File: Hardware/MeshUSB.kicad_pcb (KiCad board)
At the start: 2 copper layers, 30.4 x 40.8 mm, 37 parts, among them P1 USB_4, P2 PVCell, Q1 MOS_P, U1 XBEE, U3 LTC3105-MSOP12, U4 FT231X-SSOP, U5 LTC4070

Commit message: Getting moving on v0.2 :)
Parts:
- L1: footprint SM1210 -> SM0805
- R10: value R -> 270
- U4: footprint SSOP20 -> _MUSB_SSOP20
- moved L1 34.7 mm to (137.2, 90.2)
- moved U4 21.2 mm to (166.6, 132.8)
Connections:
- F1 pad 1: N-0000015 -> N-0000012
- P1 pad 1: N-0000015 -> GND
- P1 pad 3: N-0000012 -> N-0000014
- P1 pad 4: GND -> N-0000012
- R1 pad 1: N-0000013 -> N-0000014
- R2 pad 1: N-0000012 -> N-0000013
- VR1 pad 1: N-0000012 -> N-0000013
- VR2 pad 1: N-0000013 -> N-0000014
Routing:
- net N-0000012: track 16.9 -> 3.61 mm
- net N-0000015: track 11.9 -> 0.00 mm
- net N-0000013: track 13.5 -> 2.69 mm
- net GND: track 173.4 -> 163.5 mm
- net N-0000014: track 0.00 -> 1.14 mm

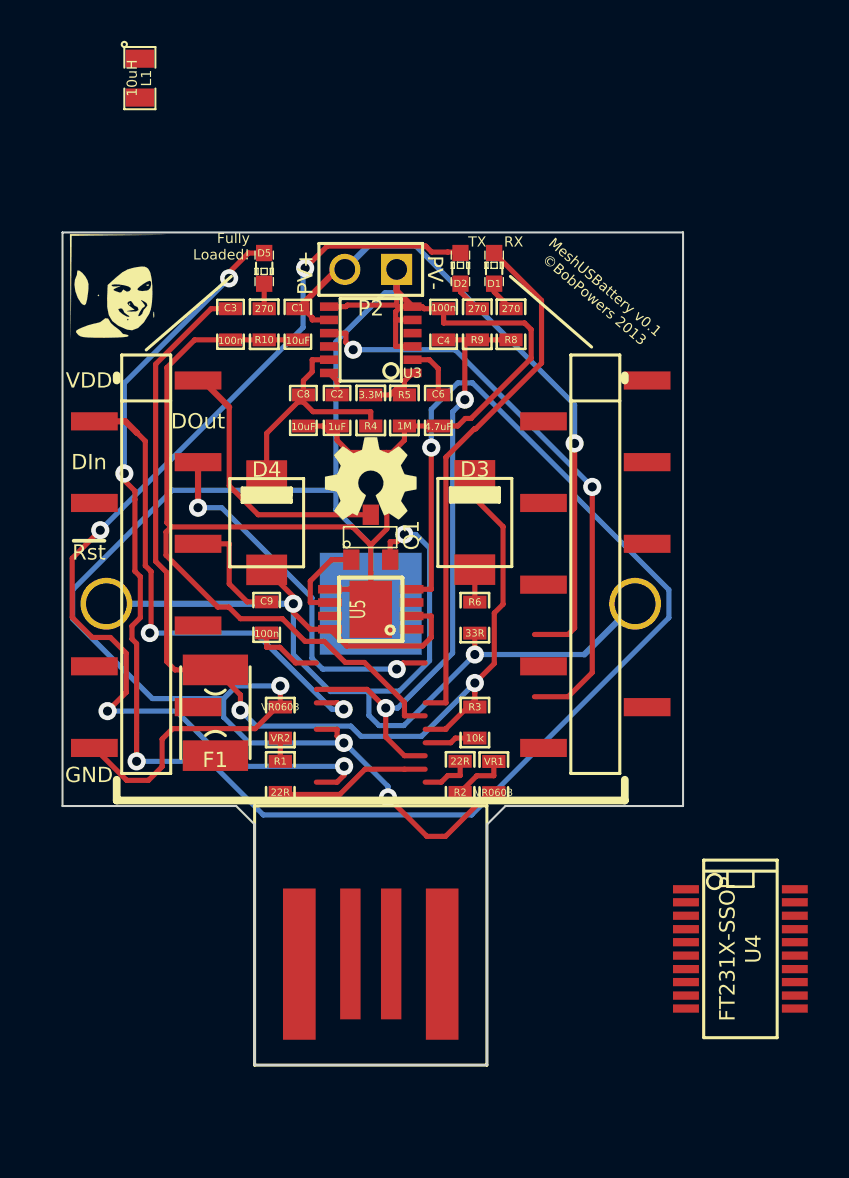
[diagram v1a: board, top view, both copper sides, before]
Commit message: More changes on list to v0.2.
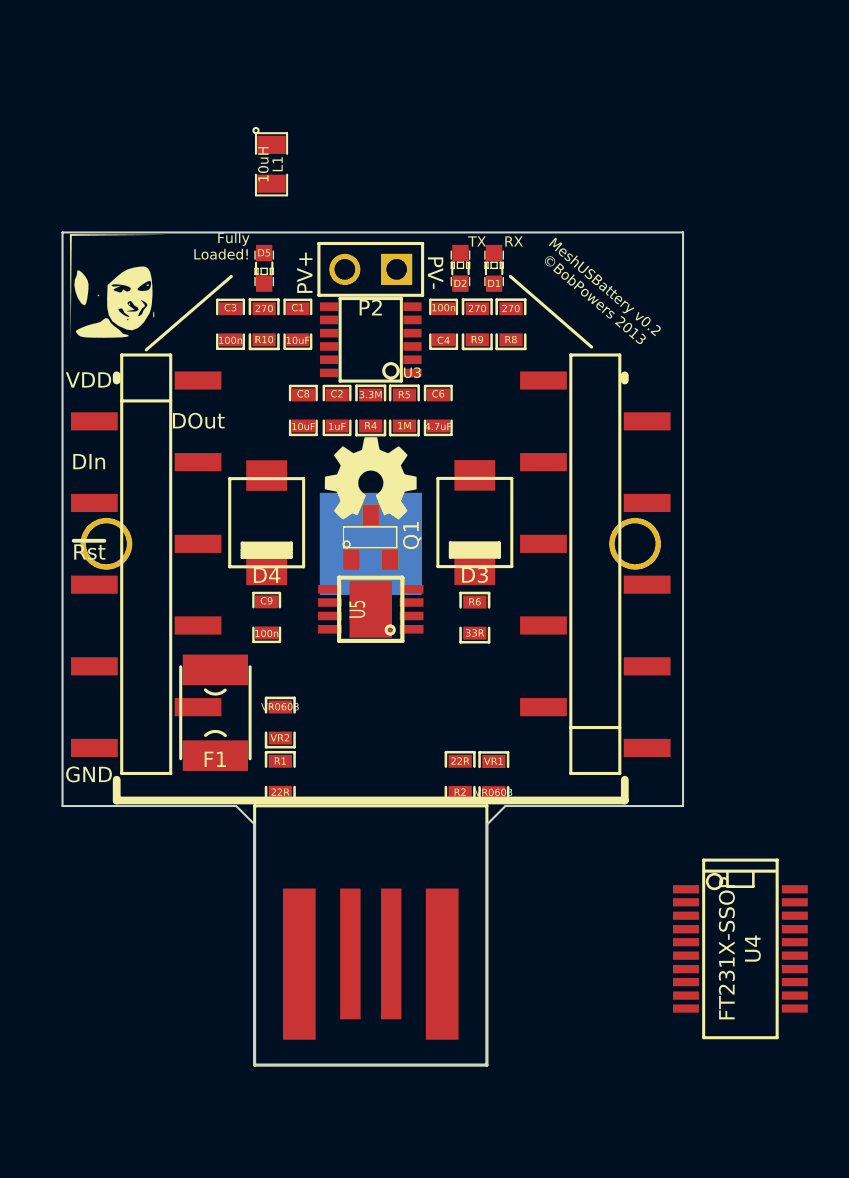
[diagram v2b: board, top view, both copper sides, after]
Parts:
- removed R3: 10k, _MUSB_SM0603_Resistor
- H1: footprint _MUSB-FEMALE-HEADER-NPPN101BFLC-RC -> _MUSB-FEMALE-HEADER-NPPN101BFLC-RC-Pin1Left
- H2: footprint _MUSB-FEMALE-HEADER-NPPN101BFLC-RC -> _MUSB-FEMALE-HEADER-NPPN101BFLD-RC-Pin1Right
- moved L1 7.71 mm to (143.6, 94.4)
- moved Li-Battery1 2.94 mm to (148.5, 113.0)
- turned D3 to 270 degrees
- turned D4 to 270 degrees
- turned H2 to 0 degrees
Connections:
- U4 pad 14: N-000008 (its old number) -> VCCIO
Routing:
- net GND: track 163.5 -> 0.00 mm, vias 3 -> 0
- net N-0000023: track 87.9 -> 0.00 mm, vias 4 -> 0
- net N-0000033: track 58.6 -> 0.00 mm, vias 3 -> 0
- net USB_VDD: track 53.3 -> 0.00 mm, vias 2 -> 0
- net N-000006: track 51.3 -> 0.00 mm, vias 4 -> 0
- net N-0000034: track 32.9 -> 0.00 mm, vias 1 -> 0
- net VCCIO: track 30.8 -> 0.00 mm, vias 2 -> 0
- net N-0000035: track 28.7 -> 0.00 mm, vias 2 -> 0
- net N-000001: track 26.0 -> 0.00 mm
- net N-000003: track 25.0 -> 0.00 mm, vias 2 -> 0
- net N-000002: track 18.5 -> 0.00 mm, vias 2 -> 0
- net BAT+: track 13.4 -> 0.00 mm
- net N-0000036: track 11.8 -> 0.00 mm
- net N-0000010: track 7.65 -> 0.00 mm
- net N-000005: track 5.69 -> 0.00 mm
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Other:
- board text added: "MeshUSBattery v0.2 ©BobPowers 2013"
- board text removed: "MeshUSBattery v0.1 ©BobPowers 2013"

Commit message: Almost everything on the TODO is done. Layout done.
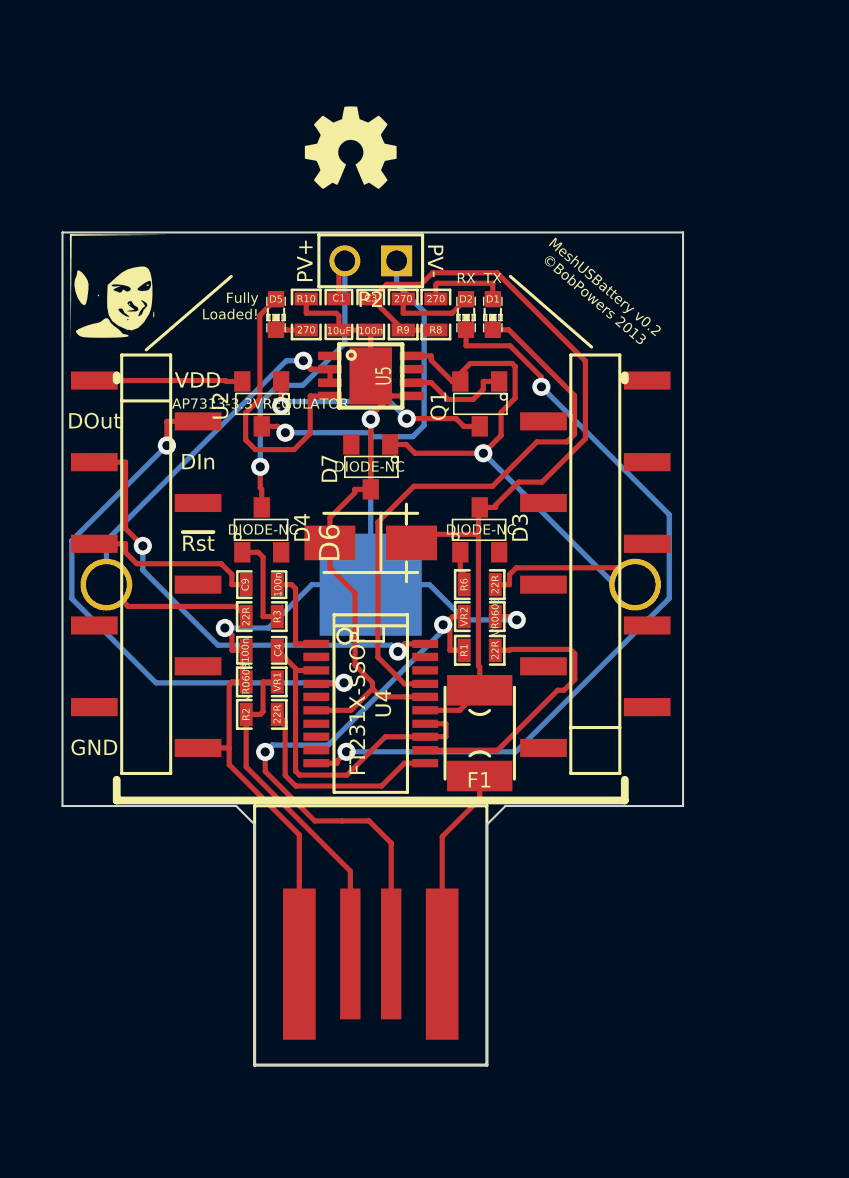
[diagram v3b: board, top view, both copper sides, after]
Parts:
- removed C2: 1uF, _MUSB_SM0603_Capa
- removed C6: 4.7uF, _MUSB_SM0603_Capa
- removed C8: 10uF, _MUSB_SM0603_Capa
- removed L1: 10uH, SM0805
- removed R4: 3.3M, _MUSB_SM0603_Resistor
- removed R5: 1M, _MUSB_SM0603_Resistor
- removed U3: LTC3105-MSOP12, _MUSB_MSOP12
- added D6: ZENER, _MUSB_SMAZ5V6-Zener-DO214, F.Cu at (148.5, 113.0)
- added D7: DIODE-NC, SOT23, F.Cu at (148.5, 109.2)
- added R3: 22R, _MUSB_SM0603_Resistor, F.Cu at (143.2, 116.6)
- added U2: AP7313-3.3VREGULATOR, SOT23, F.Cu at (143.2, 106.2)
- D3, D4: value DIODESCH -> DIODE-NC; footprint _MUSB_DO-214BA-Schottky -> SOT23
- H1: footprint _MUSB-FEMALE-HEADER-NPPN101BFLC-RC-Pin1Left -> _MUSB-FEMALE-HEADER-NPPN101BFLD-RC-Pin1Right
- H2: footprint _MUSB-FEMALE-HEADER-NPPN101BFLD-RC-Pin1Right -> _MUSB-FEMALE-HEADER-NPPN101BFLC-RC-Pin1Left
- R6: value 33R -> 22R
- moved U4 21.7 mm to (148.5, 120.8)
- moved C4 18.3 mm to (143.2, 118.2), turned to 180 degrees
- moved G1 16.2 mm to (147.5, 93.6)
- moved F1 13.0 mm to (153.8, 122.3)
- moved VR1 12.3 mm to (143.2, 119.8), turned to 180 degrees
- moved R1 11.6 mm to (153.8, 118.2), turned to 0 degrees
- moved U5 11.4 mm to (148.5, 104.8), turned to 270 degrees
- moved VR2 11.1 mm to (153.8, 116.6), turned to 0 degrees
- moved R2 10.2 mm to (143.2, 121.4), turned to 0 degrees
- moved Q1 8.43 mm to (153.8, 106.2), turned to 180 degrees
- moved C3 6.89 mm to (148.5, 101.8)
- moved R8 3.71 mm to (151.7, 101.8)
- moved R9 3.66 mm to (150.1, 101.8)
- moved D5 2.33 mm to (143.9, 101.8)
- moved D2 2.28 mm to (153.2, 101.8), turned to 270 degrees
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- renumbered G*** to G0, G*** to G1
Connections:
- C1 pad 1: N-0000034 (its old number) -> N-0000018
- D3 pad 1: USB_VDD -> N-0000024
- D3 pad 2: N-0000015 -> N-0000022
- D4 pad 2: N-0000033 (its old number) -> N-0000021
- Li-Battery1 pad 1: N-0000033 (its old number) -> N-0000019
- P2 pad 2: N-0000034 (its old number) -> N-0000018
- Q1 pad 2: N-0000033 (its old number) -> N-0000019
- Q1 pad 3: BAT+ -> N-0000017
- R6 pad 1: N-0000015 -> N-0000024
- R6 pad 2: N-0000033 (its old number) -> N-0000019
- R8 pad 1: VCCIO -> USB_VDD
- R9 pad 1: VCCIO -> USB_VDD
- U5 pad 2: N-0000033 (its old number) -> N-0000019
- U5 pad 3: N-0000017 -> N-0000019
- U5 pad 8: N-0000033 (its old number) -> N-0000019
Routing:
- net GND: track 0.00 -> 95.2 mm, vias 0 -> 4
- net N-0000019: track 0.00 -> 59.2 mm, vias 0 -> 2
- net USB_VDD: track 0.00 -> 42.6 mm
- net N-000001: track 0.00 -> 39.2 mm, vias 0 -> 2
- net N-000009: track 0.00 -> 28.8 mm, vias 0 -> 2
- net N-000003: track 0.00 -> 28.6 mm, vias 0 -> 2
- net N-000006: track 0.00 -> 28.1 mm
- net N-000002: track 0.00 -> 22.8 mm, vias 0 -> 2
- net VCCIO: track 0.00 -> 17.2 mm
- net N-0000010: track 0.00 -> 16.9 mm
- net N-0000018: track 0.00 -> 16.5 mm, vias 0 -> 1
- net N-0000011: track 0.00 -> 14.0 mm
- net N-0000026: track 0.00 -> 14.0 mm
- net N-0000017: track 0.00 -> 11.5 mm, vias 0 -> 2
- net N-0000012: track 0.00 -> 10.7 mm
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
